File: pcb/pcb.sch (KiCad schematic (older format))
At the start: 2 parts

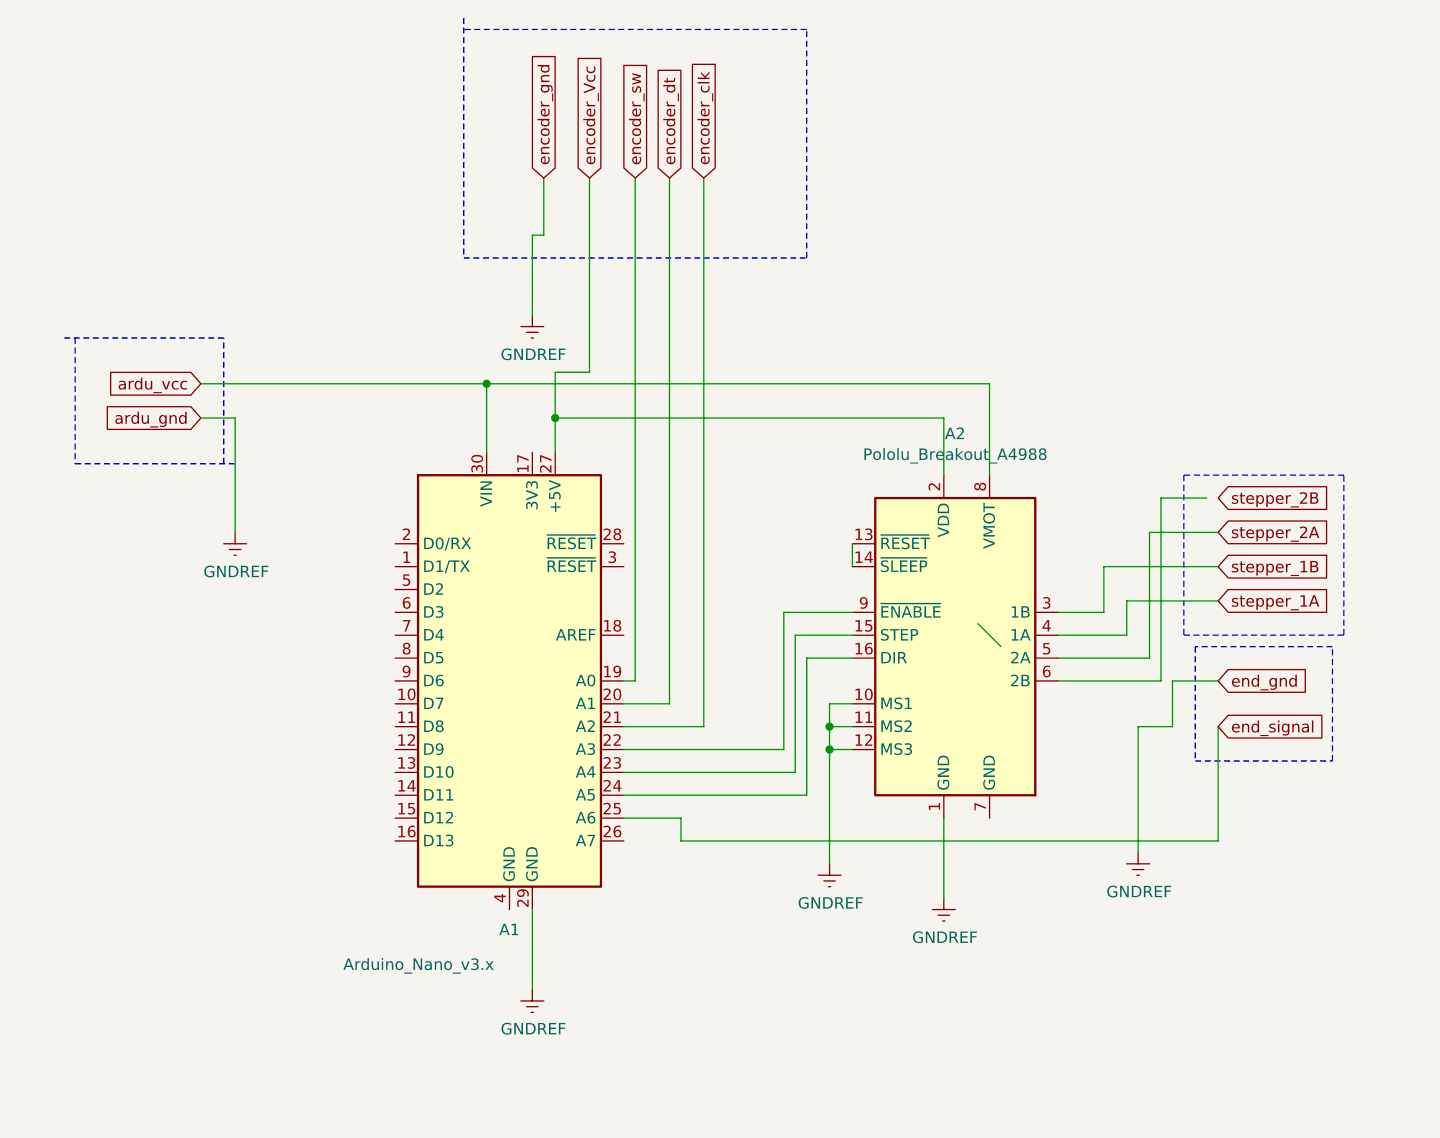
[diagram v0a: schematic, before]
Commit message: add display support
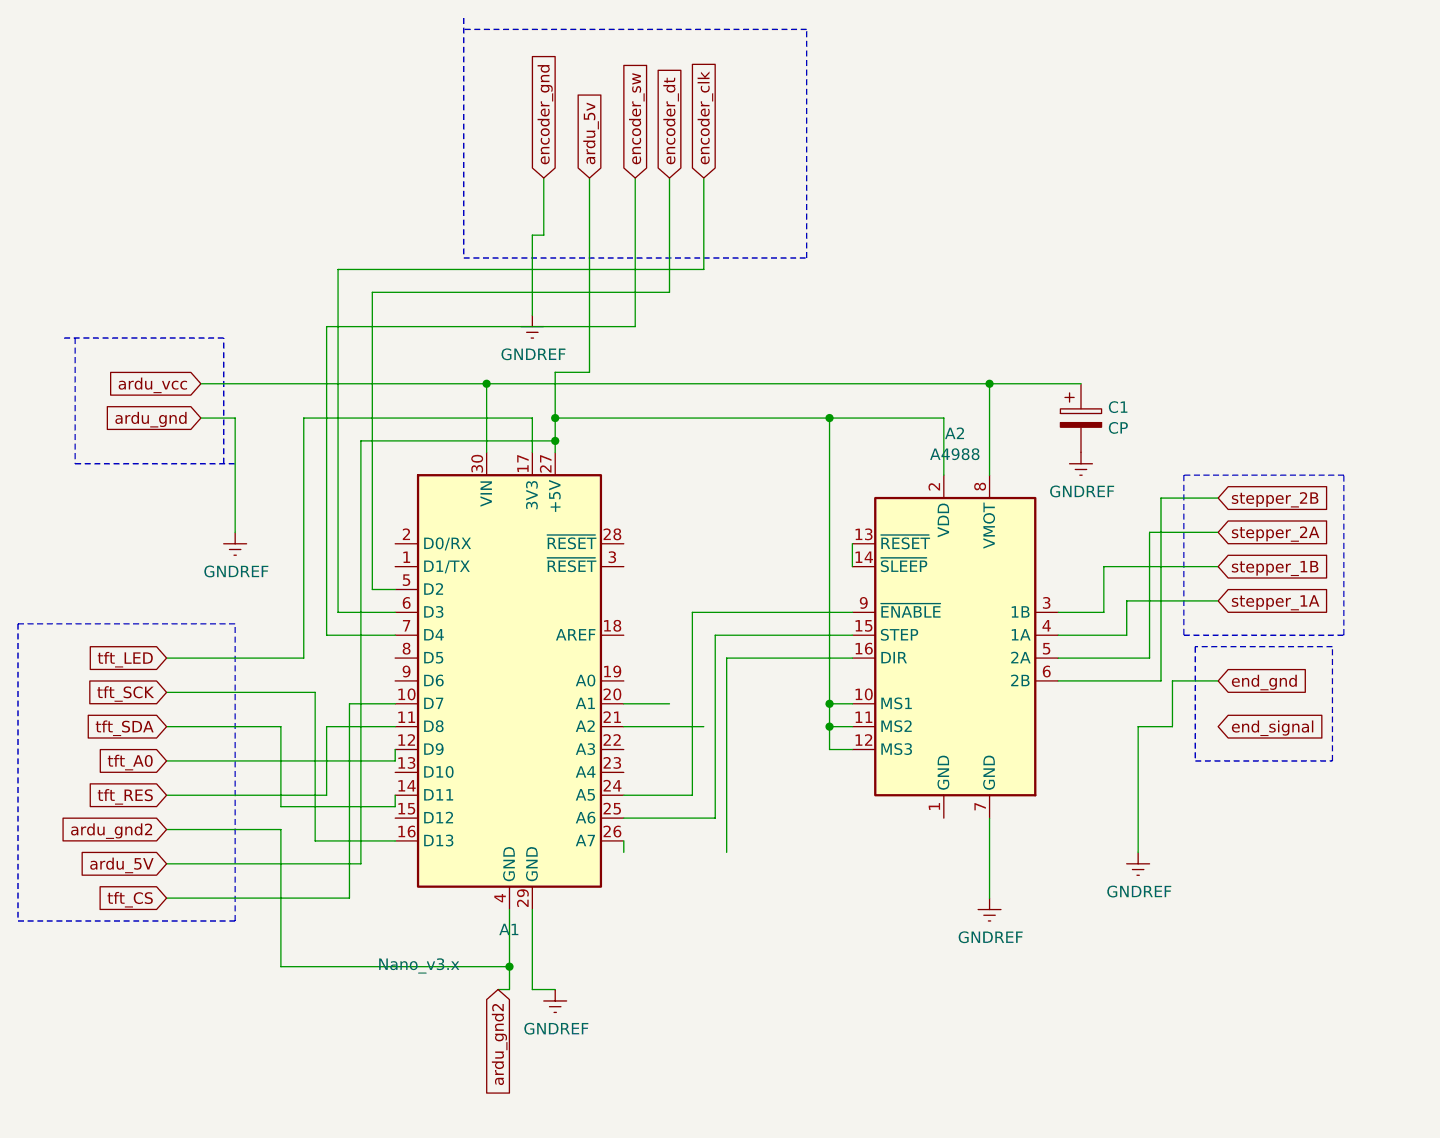
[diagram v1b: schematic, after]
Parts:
- added C1: CP, Capacitor_THT:CP_Radial_D5.0mm_P2.00mm, symbol Device:CP
- A1: value Arduino_Nano_v3.x -> Nano_v3.x
- A2: value Pololu_Breakout_A4988 -> A4988
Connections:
- net labels added: ardu_5V, ardu_5v, ardu_gnd2, tft_A0, tft_CS, tft_LED, tft_RES, tft_SCK, tft_SDA
- net labels removed: encoder_Vcc
- wire segments 59 -> 95
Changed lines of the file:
@@
 Comment4 ""
 $EndDescr
-$Comp
-L Driver_Motor:Pololu_Breakout_A4988 A2
-U 1 1 6164C436
-P 5250 3600
-F 0 "A2" H 5300 4481 50  0000 C CNN
-F 1 "Pololu_Breakout_A4988" H 5300 4390 50  0000 C CNN
-F 2 "Module:Pololu_Breakout-16_15.2x20.3mm" H 5525 2850 50  0001 L CNN
-F 3 "https://www.pololu.com/product/2980/pictures" H 5350 3300 50  0001 C CNN
-	1    5250 3600
-	1    0    0    -1
-$EndComp
 Text GLabel 4200 1600 1    50   Input ~ 0
 encoder_clk
@@
 encoder_sw
 Text GLabel 3700 1600 1    50   Input ~ 0
-encoder_Vcc
+ardu_5v
 Text GLabel 3500 1600 1    50   Input ~ 0
 encoder_gnd
@@
 Text GLabel 6450 3150 2    50   Input ~ 0
 stepper_2A
-Text GLabel 6450 3000 2    50   Input ~ 0
-stepper_2B
 Wire Notes Line
 	6300 2900 6300 3600
@@
 	3550 2450 3550 2650
 Wire Wire Line
-	3900 1600 3900 3800
-Wire Wire Line
-	3900 3800 3850 3800
-Wire Wire Line
-	4050 1600 4050 3900
-Wire Wire Line
-	4050 3900 3850 3900
-Wire Wire Line
-	4200 1600 4200 4000
-Wire Wire Line
-	4200 4000 3850 4000
-Wire Wire Line
 	4850 3300 4850 3200
 Wire Wire Line
@@
 	5250 2900 5250 2650
 Wire Wire Line
-	5250 2650 3550 2650
+	5250 2650 4750 2650
 Connection ~ 3550 2650
 Wire Wire Line
-	3550 2650 3550 2800
-Wire Wire Line
-	3850 4100 4550 4100
-Wire Wire Line
-	4550 4100 4550 3500
-Wire Wire Line
-	4550 3500 4850 3500
-Wire Wire Line
-	3850 4200 4600 4200
-Wire Wire Line
-	4600 4200 4600 3600
-Wire Wire Line
-	4600 3600 4850 3600
-Wire Wire Line
-	4850 3700 4650 3700
-Wire Wire Line
-	4650 3700 4650 4300
-Wire Wire Line
-	4650 4300 3850 4300
-$Comp
-L power:GNDREF #PWR0101
-U 1 1 616553A5
-P 4750 4600
-F 0 "#PWR0101" H 4750 4350 50  0001 C CNN
-F 1 "GNDREF" H 4755 4427 50  0000 C CNN
-F 2 "" H 4750 4600 50  0001 C CNN
-F 3 "" H 4750 4600 50  0001 C CNN
-	1    4750 4600
-	1    0    0    -1
-$EndComp
-Wire Wire Line
-	4750 4600 4750 4100
-Wire Wire Line
-	4750 3900 4850 3900
-Wire Wire Line
-	4850 4000 4750 4000
+	3550 2650 3550 2750
 Connection ~ 4750 4000
 Wire Wire Line
 	4750 4000 4750 3900
-Wire Wire Line
-	4850 4100 4750 4100
-Connection ~ 4750 4100
 Wire Wire Line
 	4750 4100 4750 4000
@@
 L power:GNDREF #PWR0102
 U 1 1 61656CBC
-P 3450 5150
-F 0 "#PWR0102" H 3450 4900 50  0001 C CNN
-F 1 "GNDREF" H 3455 4977 50  0000 C CNN
-F 2 "" H 3450 5150 50  0001 C CNN
-F 3 "" H 3450 5150 50  0001 C CNN
-	1    3450 5150
+P 3550 5150
+F 0 "#PWR0102" H 3550 4900 50  0001 C CNN
+F 1 "GNDREF" H 3555 4977 50  0000 C CNN
+F 2 "" H 3550 5150 50  0001 C CNN
+F 3 "" H 3550 5150 50  0001 C CNN
+	1    3550 5150
 	1    0    0    -1
 $EndComp
@@
 	1    0    0    -1
 $EndComp
+Wire Wire Line
+	2000 2650 2150 2650
+Wire Wire Line
+	2150 2650 2150 3150
+Wire Wire Line
+	3450 1850 3500 1850
+Wire Wire Line
+	3500 1850 3500 1600
+Wire Wire Line
+	5950 3500 5950 3300
+Wire Wire Line
+	5950 3300 6450 3300
+Wire Wire Line
+	6450 3450 6050 3450
+Wire Wire Line
+	6050 3450 6050 3600
+Wire Wire Line
+	6050 3600 5750 3600
+Wire Wire Line
+	6450 3150 6150 3150
+Wire Wire Line
+	6150 3150 6150 3700
+Wire Wire Line
+	6150 3700 5750 3700
+$Comp
+L power:GNDREF #PWR0105
+U 1 1 6165E54D
+P 6100 4550
+F 0 "#PWR0105" H 6100 4300 50  0001 C CNN
+F 1 "GNDREF" H 6105 4377 50  0000 C CNN
+F 2 "" H 6100 4550 50  0001 C CNN
+F 3 "" H 6100 4550 50  0001 C CNN
+	1    6100 4550
+	1    0    0    -1
+$EndComp
+Wire Wire Line
+	6100 4550 6100 4000
+Wire Wire Line
+	6100 4000 6250 4000
+Wire Wire Line
+	6250 4000 6250 3800
+Wire Wire Line
+	6250 3800 6450 3800
+$Comp
+L power:GNDREF #PWR0106
+U 1 1 61660AED
+P 5450 4750
+F 0 "#PWR0106" H 5450 4500 50  0001 C CNN
+F 1 "GNDREF" H 5455 4577 50  0000 C CNN
+F 2 "" H 5450 4750 50  0001 C CNN
+F 3 "" H 5450 4750 50  0001 C CNN
+	1    5450 4750
+	1    0    0    -1
+$EndComp
+Wire Wire Line
+	4200 4000 3850 4000
+Wire Wire Line
+	4050 3900 3850 3900
+Wire Wire Line
+	3450 4800 3450 5150
+Wire Wire Line
+	3450 5150 3550 5150
+Wire Wire Line
+	5750 3500 5950 3500
+Wire Wire Line
+	5450 4750 5450 4400
+Wire Wire Line
+	4850 4100 4750 4100
+Wire Wire Line
+	4850 4000 4750 4000
+Wire Wire Line
+	4750 3900 4850 3900
+$Comp
+L Driver_Motor:Pololu_Breakout_A4988 A2
+U 1 1 6164C436
+P 5250 3600
+F 0 "A2" H 5300 4481 50  0000 C CNN
+F 1 "A4988" H 5300 4390 50  0000 C CNN
+F 2 "Module:Pololu_Breakout-16_15.2x20.3mm" H 5525 2850 50  0001 L CNN
+F 3 "https://www.pololu.com/product/2980/pictures" H 5350 3300 50  0001 C CNN
+	1    5250 3600
+	1    0    0    -1
+$EndComp
+Connection ~ 4750 3900
+Connection ~ 4750 2650
+Wire Wire Line
+	4750 2650 3550 2650
+Wire Wire Line
+	6450 3000 6200 3000
+Wire Wire Line
+	6200 3000 6200 3800
+Wire Wire Line
+	6200 3800 5750 3800
+Text GLabel 6450 3000 2    50   Input ~ 0
+stepper_2B
+Wire Wire Line
+	4750 3900 4750 2650
 $Comp
 L MCU_Module:Arduino_Nano_v3.x A1
@@
 P 3350 3800
 F 0 "A1" H 3350 2711 50  0000 C CNN
-F 1 "Arduino_Nano_v3.x" H 2953 2559 50  0000 C CNN
+F 1 "Nano_v3.x" H 2953 2559 50  0000 C CNN
 F 2 "Module:Arduino_Nano" H 3350 3800 50  0001 C CIN
 F 3 "http://www.mouser.com/pdfdocs/Gravitech_Arduino_Nano3_0.pdf" H 3350 3800 50  0001 C CNN
@@
 $EndComp
 Wire Wire Line
-	3450 4800 3450 5150
-Entry Wire Line
-	5400 3550 5500 3650
-Wire Wire Line
-	2000 2650 2150 2650
-Wire Wire Line
-	2150 2650 2150 3150
+	4850 3700 4300 3700
+Wire Wire Line
+	4300 3700 4300 4550
+Wire Wire Line
+	3850 4550 3850 4500
+Wire Wire Line
+	3850 4400 4250 4400
+Wire Wire Line
+	4250 4400 4250 3600
+Wire Wire Line
+	4250 3600 4850 3600
+Wire Wire Line
+	4850 3500 4150 3500
+Wire Wire Line
+	4150 3500 4150 4300
+Wire Wire Line
+	4150 4300 3850 4300
+$Comp
+L Device:CP C1
+U 1 1 616E050A
+P 5850 2650
+F 0 "C1" H 5968 2696 50  0000 L CNN
+F 1 "CP" H 5968 2605 50  0000 L CNN
+F 2 "Capacitor_THT:CP_Radial_D5.0mm_P2.00mm" H 5888 2500 50  0001 C CNN
+F 3 "~" H 5850 2650 50  0001 C CNN
+	1    5850 2650
+	1    0    0    -1
+$EndComp
+Wire Wire Line
+	5450 2500 5850 2500
+Connection ~ 5450 2500
+$Comp
+L power:GNDREF #PWR0101
+U 1 1 616E3C5C
+P 5850 2800
+F 0 "#PWR0101" H 5850 2550 50  0001 C CNN
+F 1 "GNDREF" H 5855 2627 50  0000 C CNN
+F 2 "" H 5850 2800 50  0001 C CNN
+F 3 "" H 5850 2800 50  0001 C CNN
+	1    5850 2800
+	1    0    0    -1
+$EndComp
+Wire Wire Line
+	4050 1600 4050 2100
+Wire Wire Line
+	4050 2100 2750 2100
+Wire Wire Line
+	2750 2100 2750 3400
+Wire Wire Line
+	2750 3400 2850 3400
+Wire Wire Line
+	3450 2200 3450 1850
 $Comp
 L power:GNDREF #PWR0104
@@
 $EndComp
 Wire Wire Line
-	3450 2200 3450 1850
-Wire Wire Line
-	3450 1850 3500 1850
-Wire Wire Line
-	3500 1850 3500 1600
-Wire Wire Line
-	5750 3500 5950 3500
-Wire Wire Line
-	5950 3500 5950 3300
-Wire Wire Line
-	5950 3300 6450 3300
-Wire Wire Line
-	6450 3450 6050 3450
-Wire Wire Line
-	6050 3450 6050 3600
-Wire Wire Line
-	6050 3600 5750 3600
-Wire Wire Line
-	6450 3150 6150 3150
-Wire Wire Line
-	6150 3150 6150 3700
-Wire Wire Line
-	6150 3700 5750 3700
-Wire Wire Line
-	6400 3000 6200 3000
-Wire Wire Line
-	6200 3000 6200 3800
-Wire Wire Line
-	6200 3800 5750 3800
-$Comp
-L power:GNDREF #PWR0105
-U 1 1 6165E54D
-P 6100 4550
-F 0 "#PWR0105" H 6100 4300 50  0001 C CNN
-F 1 "GNDREF" H 6105 4377 50  0000 C CNN
-F 2 "" H 6100 4550 50  0001 C CNN
-F 3 "" H 6100 4550 50  0001 C CNN
-	1    6100 4550
-	1    0    0    -1
-$EndComp
-Wire Wire Line
-	6100 4550 6100 4000
-Wire Wire Line
-	6100 4000 6250 4000
-Wire Wire Line
-	6250 4000 6250 3800
-Wire Wire Line
-	6250 3800 6450 3800
-Wire Wire Line
-	6450 4000 6450 4500
-Wire Wire Line
-	6450 4500 4100 4500
-Wire Wire Line
-	4100 4500 4100 4400
-Wire Wire Line
-	4100 4400 3850 4400
-$Comp
-L power:GNDREF #PWR0106
-U 1 1 61660AED
-P 5250 4750
-F 0 "#PWR0106" H 5250 4500 50  0001 C CNN
-F 1 "GNDREF" H 5255 4577 50  0000 C CNN
-F 2 "" H 5250 4750 50  0001 C CNN
-F 3 "" H 5250 4750 50  0001 C CNN
-	1    5250 4750
-	1    0    0    -1
-$EndComp
-Wire Wire Line
-	5250 4750 5250 4400
+	4200 1600 4200 2000
+Wire Wire Line
+	4200 2000 2600 2000
+Wire Wire Line
+	2600 2000 2600 3500
+Wire Wire Line
+	2600 3500 2850 3500
+Text GLabel 3300 5150 3    50   Input ~ 0
+ardu_gnd2
+Wire Wire Line
+	3350 4800 3350 5050
+Wire Wire Line
+	3350 5150 3300 5150
+Text GLabel 1850 3700 0    50   Input ~ 0
+tft_LED
+Text GLabel 1850 3850 0    50   Input ~ 0
+tft_SCK
+Text GLabel 1850 4000 0    50   Input ~ 0
+tft_SDA
+Text GLabel 1850 4150 0    50   Input ~ 0
+tft_A0
+Text GLabel 1850 4300 0    50   Input ~ 0
+tft_RES
+Text GLabel 1850 4450 0    50   Input ~ 0
+ardu_gnd2
+Text GLabel 1850 4600 0    50   Input ~ 0
+ardu_5V
+Wire Notes Line
+	1200 3550 1200 4850
+Wire Notes Line
+	1200 4850 2150 4850
+Wire Notes Line
+	2150 4850 2150 3550
+Wire Notes Line
+	2150 3550 1200 3550
+Wire Wire Line
+	3350 5050 2350 5050
+Wire Wire Line
+	2350 5050 2350 4450
+Wire Wire Line
+	2350 4450 1850 4450
+Connection ~ 3350 5050
+Wire Wire Line
+	3350 5050 3350 5150
+Wire Wire Line
+	1850 4600 2700 4600
+Wire Wire Line
+	2700 4600 2700 2750
+Wire Wire Line
+	2700 2750 3550 2750
+Connection ~ 3550 2750
+Wire Wire Line
+	3550 2750 3550 2800
+Wire Wire Line
+	1850 4300 2550 4300
+Wire Wire Line
+	2550 4300 2550 4000
+Wire Wire Line
+	2550 4000 2850 4000
+Wire Wire Line
+	2850 4150 2850 4100
+Wire Wire Line
+	1850 4000 2350 4000
+Wire Wire Line
+	2350 4000 2350 4350
+Wire Wire Line
+	2350 4350 2850 4350
+Wire Wire Line
+	2850 4350 2850 4300
+Wire Wire Line
+	1850 3850 2500 3850
+Wire Wire Line
+	2500 3850 2500 4500
+Wire Wire Line
+	2500 4500 2850 4500
+Wire Wire Line
+	1850 3700 2450 3700
+Wire Wire Line
+	2450 3700 2450 2650
+Wire Wire Line
+	2450 2650 3450 2650
+Wire Wire Line
+	3450 2650 3450 2800
+Wire Wire Line
+	3900 1600 3900 2250
+Wire Wire Line
+	3900 2250 2550 2250
+Wire Wire Line
+	2550 2250 2550 3600
+Wire Wire Line
+	2550 3600 2850 3600
+Text GLabel 1850 4750 0    50   Input ~ 0
+tft_CS
+Wire Wire Line
+	1850 4750 2650 4750
+Wire Wire Line
+	1850 4150 2850 4150
+Wire Wire Line
+	2650 4750 2650 3900
+Wire Wire Line
+	2650 3900 2850 3900
 $EndSCHEMATC

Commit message: update pcb
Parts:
- added Q1: 2N3906, Package_TO_SOT_THT:TO-92_Inline, symbol Transistor_BJT:2N3906
- added R1: R, Resistor_THT:R_Axial_DIN0204_L3.6mm_D1.6mm_P5.08mm_Horizontal, symbol Device:R
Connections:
- wire segments 95 -> 106
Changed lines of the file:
@@
 Wire Wire Line
 	6250 3800 6450 3800
-$Comp
-L power:GNDREF #PWR0106
-U 1 1 61660AED
-P 5450 4750
-F 0 "#PWR0106" H 5450 4500 50  0001 C CNN
-F 1 "GNDREF" H 5455 4577 50  0000 C CNN
-F 2 "" H 5450 4750 50  0001 C CNN
-F 3 "" H 5450 4750 50  0001 C CNN
-	1    5450 4750
-	1    0    0    -1
-$EndComp
-Wire Wire Line
-	4200 4000 3850 4000
-Wire Wire Line
-	4050 3900 3850 3900
 Wire Wire Line
 	3450 4800 3450 5150
@@
 Wire Wire Line
 	5750 3500 5950 3500
-Wire Wire Line
-	5450 4750 5450 4400
 Wire Wire Line
 	4850 4100 4750 4100
@@
 Wire Wire Line
 	4750 3900 4750 2650
-$Comp
-L MCU_Module:Arduino_Nano_v3.x A1
-U 1 1 6164E403
-P 3350 3800
-F 0 "A1" H 3350 2711 50  0000 C CNN
-F 1 "Nano_v3.x" H 2953 2559 50  0000 C CNN
-F 2 "Module:Arduino_Nano" H 3350 3800 50  0001 C CIN
-F 3 "http://www.mouser.com/pdfdocs/Gravitech_Arduino_Nano3_0.pdf" H 3350 3800 50  0001 C CNN
-	1    3350 3800
-	1    0    0    -1
-$EndComp
 Wire Wire Line
 	4850 3700 4300 3700
 Wire Wire Line
-	4300 3700 4300 4550
-Wire Wire Line
-	3850 4550 3850 4500
-Wire Wire Line
-	3850 4400 4250 4400
-Wire Wire Line
-	4250 4400 4250 3600
+	4300 3700 4300 4300
 Wire Wire Line
 	4250 3600 4850 3600
-Wire Wire Line
-	4850 3500 4150 3500
-Wire Wire Line
-	4150 3500 4150 4300
-Wire Wire Line
-	4150 4300 3850 4300
 $Comp
 L Device:CP C1
@@
 Wire Wire Line
 	2650 3900 2850 3900
+Wire Wire Line
+	6450 4000 6300 4000
+Wire Wire Line
+	6300 4000 6300 4500
+Wire Wire Line
+	6300 4500 4400 4500
+Wire Wire Line
+	4400 4000 3900 4000
+Wire Wire Line
+	4400 4000 4400 4500
+Wire Wire Line
+	4250 4200 4250 3600
+Wire Wire Line
+	3850 4300 4300 4300
+Wire Wire Line
+	3850 4200 4250 4200
+$Comp
+L MCU_Module:Arduino_Nano_v3.x A1
+U 1 1 6164E403
+P 3350 3800
+F 0 "A1" H 3350 2711 50  0000 C CNN
+F 1 "Nano_v3.x" H 2953 2559 50  0000 C CNN
+F 2 "Module:Arduino_Nano" H 3350 3800 50  0001 C CIN
+F 3 "http://www.mouser.com/pdfdocs/Gravitech_Arduino_Nano3_0.pdf" H 3350 3800 50  0001 C CNN
+	1    3350 3800
+	1    0    0    -1
+$EndComp
+$Comp
+L Transistor_BJT:2N3906 Q1
+U 1 1 61744453
+P 4200 3000
+F 0 "Q1" H 4390 3046 50  0000 L CNN
+F 1 "2N3906" H 4390 2955 50  0000 L CNN
+F 2 "Package_TO_SOT_THT:TO-92_Inline" H 4400 2925 50  0001 L CIN
+F 3 "https://www.fairchildsemi.com/datasheets/2N/2N3906.pdf" H 4200 3000 50  0001 L CNN
+	1    4200 3000
+	1    0    0    -1
+$EndComp
+Wire Wire Line
+	4100 3000 4000 3000
+Wire Wire Line
+	4000 3000 4000 3200
+Connection ~ 4000 3000
+Wire Wire Line
+	4000 3900 3850 3900
+$Comp
+L Device:R R1
+U 1 1 617556D0
+P 4150 3350
+F 0 "R1" V 3943 3350 50  0000 C CNN
+F 1 "R" V 4034 3350 50  0000 C CNN
+F 2 "Resistor_THT:R_Axial_DIN0204_L3.6mm_D1.6mm_P5.08mm_Horizontal" V 4080 3350 50  0001 C CNN
+F 3 "~" H 4150 3350 50  0001 C CNN
+	1    4150 3350
+	0    1    1    0
+$EndComp
+Connection ~ 4000 3350
+Wire Wire Line
+	4000 3350 4000 3900
+Text GLabel 4300 2800 1    50   Input ~ 0
+ardu_5V
+Wire Wire Line
+	5450 4750 5450 4400
+$Comp
+L power:GNDREF #PWR0106
+U 1 1 61660AED
+P 5450 4750
+F 0 "#PWR0106" H 5450 4500 50  0001 C CNN
+F 1 "GNDREF" H 5455 4577 50  0000 C CNN
+F 2 "" H 5450 4750 50  0001 C CNN
+F 3 "" H 5450 4750 50  0001 C CNN
+	1    5450 4750
+	1    0    0    -1
+$EndComp
+$Comp
+L power:GNDREF #PWR0107
+U 1 1 61765388
+P 4300 3350
+F 0 "#PWR0107" H 4300 3100 50  0001 C CNN
+F 1 "GNDREF" H 4305 3177 50  0000 C CNN
+F 2 "" H 4300 3350 50  0001 C CNN
+F 3 "" H 4300 3350 50  0001 C CNN
+	1    4300 3350
+	1    0    0    -1
+$EndComp
+$Comp
+L power:GNDREF #PWR0108
+U 1 1 6176BE49
+P 4550 3200
+F 0 "#PWR0108" H 4550 2950 50  0001 C CNN
+F 1 "GNDREF" H 4555 3027 50  0000 C CNN
+F 2 "" H 4550 3200 50  0001 C CNN
+F 3 "" H 4550 3200 50  0001 C CNN
+	1    4550 3200
+	1    0    0    -1
+$EndComp
+Wire Wire Line
+	4300 3200 4550 3200
+Wire Wire Line
+	4000 3200 4250 3200
+Wire Wire Line
+	4250 3200 4250 3250
+Wire Wire Line
+	4250 3250 4450 3250
+Wire Wire Line
+	4450 3250 4450 3500
+Wire Wire Line
+	4450 3500 4850 3500
+Connection ~ 4000 3200
+Wire Wire Line
+	4000 3200 4000 3350
 $EndSCHEMATC

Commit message: replace a4899 with l2903d; resolve merge conflicts
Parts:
- removed A2: A4988, Module:Pololu_Breakout-16_15.2x20.3mm, symbol Driver_Motor:Pololu_Breakout_A4988
- removed C1: CP, Capacitor_THT:CP_Radial_D5.0mm_P2.00mm, symbol Device:CP
- removed Q1: 2N3906, Package_TO_SOT_THT:TO-92_Inline, symbol Transistor_BJT:2N3906
- removed R1: R, Resistor_THT:R_Axial_DIN0204_L3.6mm_D1.6mm_P5.08mm_Horizontal, symbol Device:R
- added U1: L293D, Package_DIP:DIP-16_W7.62mm, symbol Driver_Motor:L293D
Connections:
- net labels added: encoder1_signal, encoder2_signal, mot_+, mot_-
- net labels removed: stepper_1A, stepper_1B, stepper_2A, stepper_2B
- wire segments 106 -> 89
